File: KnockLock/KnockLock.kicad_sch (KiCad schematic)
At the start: 42 parts, among them IC1 ESP32-C3-WROOM-02-N4, IC2 LM2575-3.3WT, IC3 MC74HC74ADTR2G, J1 2477, J2 UJ20-C-H-G-TH-P16-TR, J3 TBP04R12-500-03BE, Q1 IRLML6402TRPBF, Q2 BC547B, Q3 BC547B, U1 ADXL345BCCZ-RL7

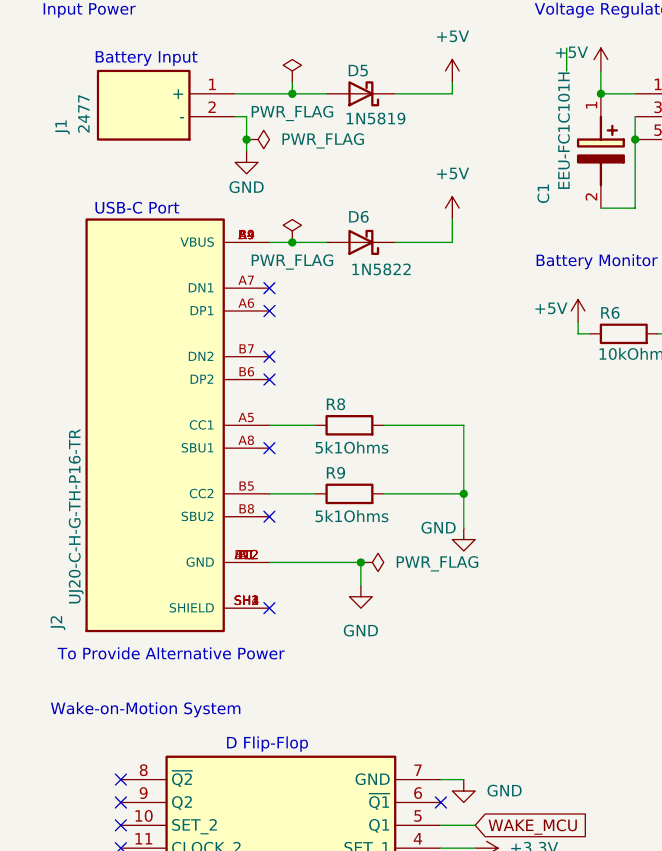
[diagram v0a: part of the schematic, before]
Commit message: Shifting to USB port, so added port and UART, but UART not connected
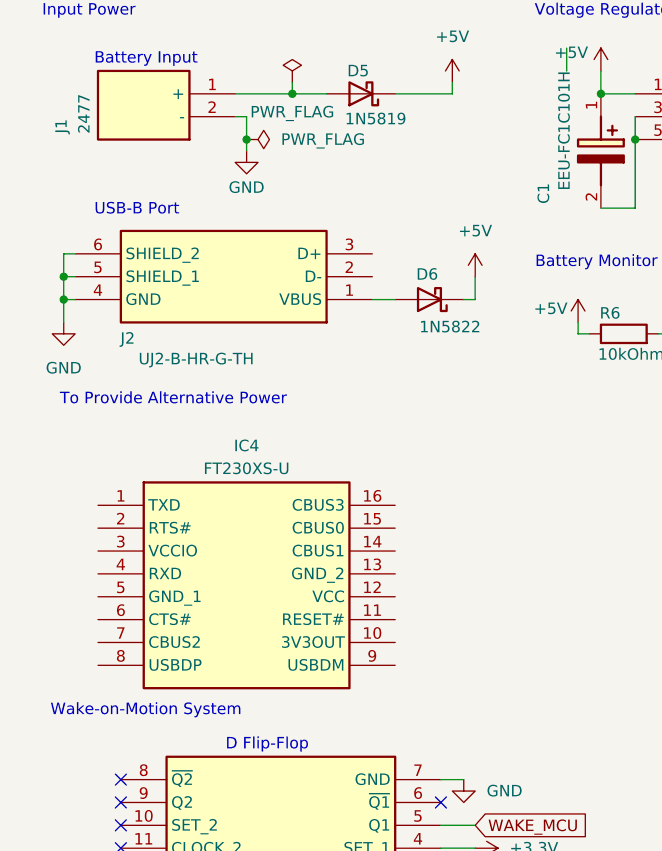
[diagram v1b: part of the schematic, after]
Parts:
- removed J2: UJ20-C-H-G-TH-P16-TR, UJ20-C-H-G-TH-P16-TR:SAMESKY_UJ20-C-H-G-TH-P16-TR, symbol UJ20-C-H-G-TH-P16-TR:UJ20-C-H-G-TH-P16-TR
- removed R8, R9: 5k1Ohms, symbol Device:R
- added IC4: FT230XS-U, SOP64P599X175-16N, symbol SamacSys_Parts:FT230XS-U
- added J2: UJ2-B-HR-G-TH, UJ2BHRGTH, symbol SamacSys_Parts:UJ2-B-HR-G-TH
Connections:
- net GND: now also J2.4 (GND), J2.5 (SHIELD_1), J2.6 (SHIELD_2)
- net at D6.2 (A): now also J2.1 (VBUS)
- no-connect marks 30 -> 23
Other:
- note added: "USB-B Port"
- note removed: "USB-C Port"
- moved on the sheet: D6

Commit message: Started Programming Interface
- we need to be careful with the IO pin logic so we can use basic buttons to enter programming mode or if we should try to use transistors (maybe also use the other side of the D flip flop)
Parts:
- added J4: UART, Connector_PinHeader_2.54mm:PinHeader_1x02_P2.54mm_Vertical, symbol Connector_Generic:Conn_01x02
- added SW1, SW2: SW_Push, symbol Switch:SW_Push
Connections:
- net FRESET: now also IC1.15 (IO3); no longer IC1.8 (IO9)
- net GND: now also SW1.1, SW2.1
- net RX: now reaches IC1.11 (RXD)
- net RX: now also J4.1 (Pin_1)
- net TX: now reaches IC1.12 (TXD)
- net TX: now also J4.2 (Pin_2)
- net MOSFET: no longer names the net of IC1.7 (IO8)
- net WAKE_MCU renamed MRESET
- net MRESET: now also SW1.2
- new net BOOT: IC1.8 (IO9), SW2.2
- no-connect marks 23 -> 21
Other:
- note added: "NPN Not Gate for Flip Flop Reset"
- note added: "Programming Interface"
- note added: "Turns off MCU"
- moved on the sheet: IC1, R1, R2

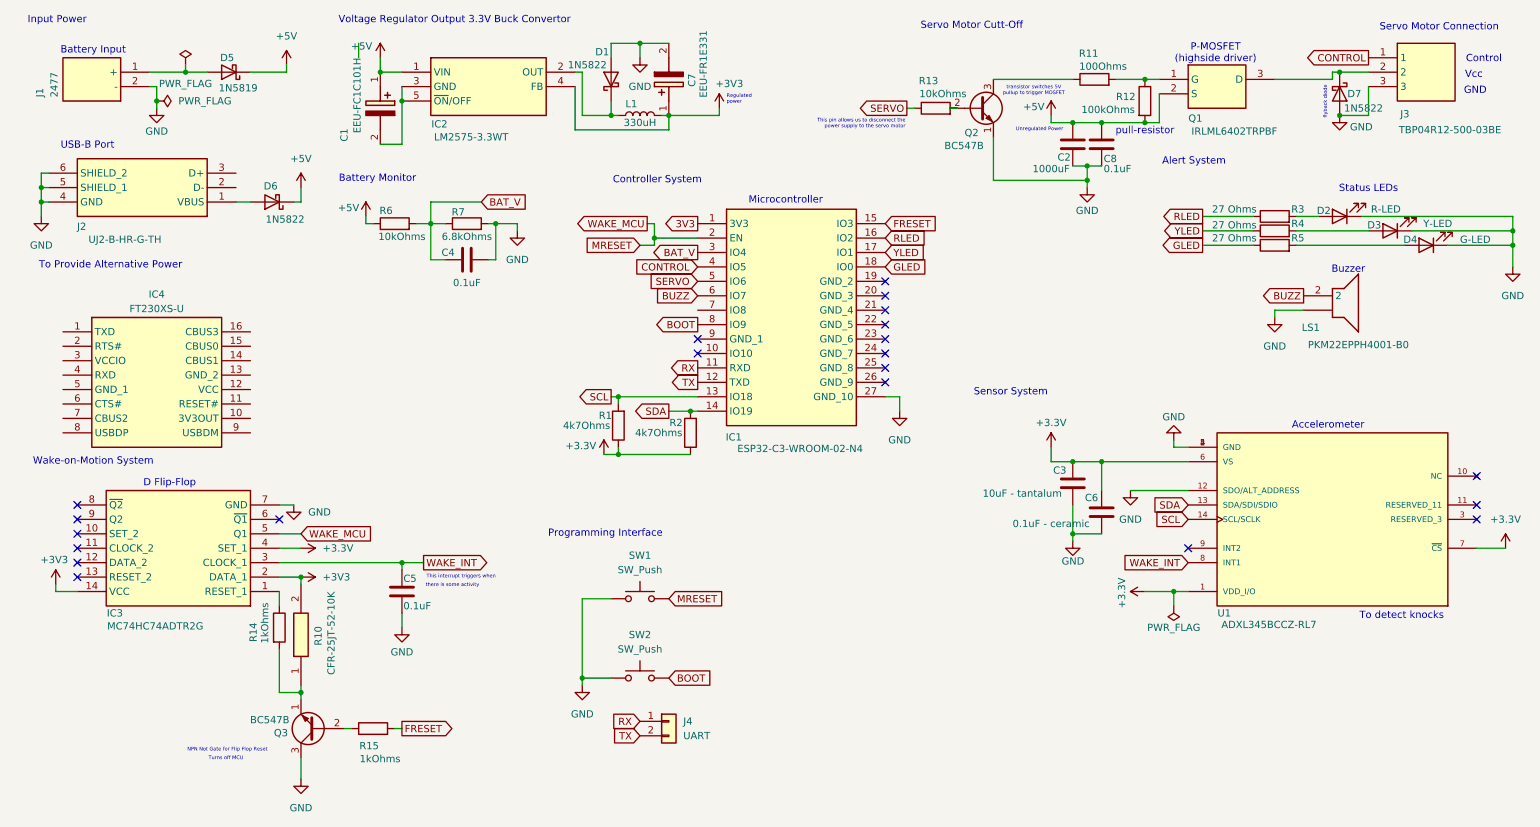
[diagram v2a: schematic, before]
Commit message: Reorganized, fixed pwr flags
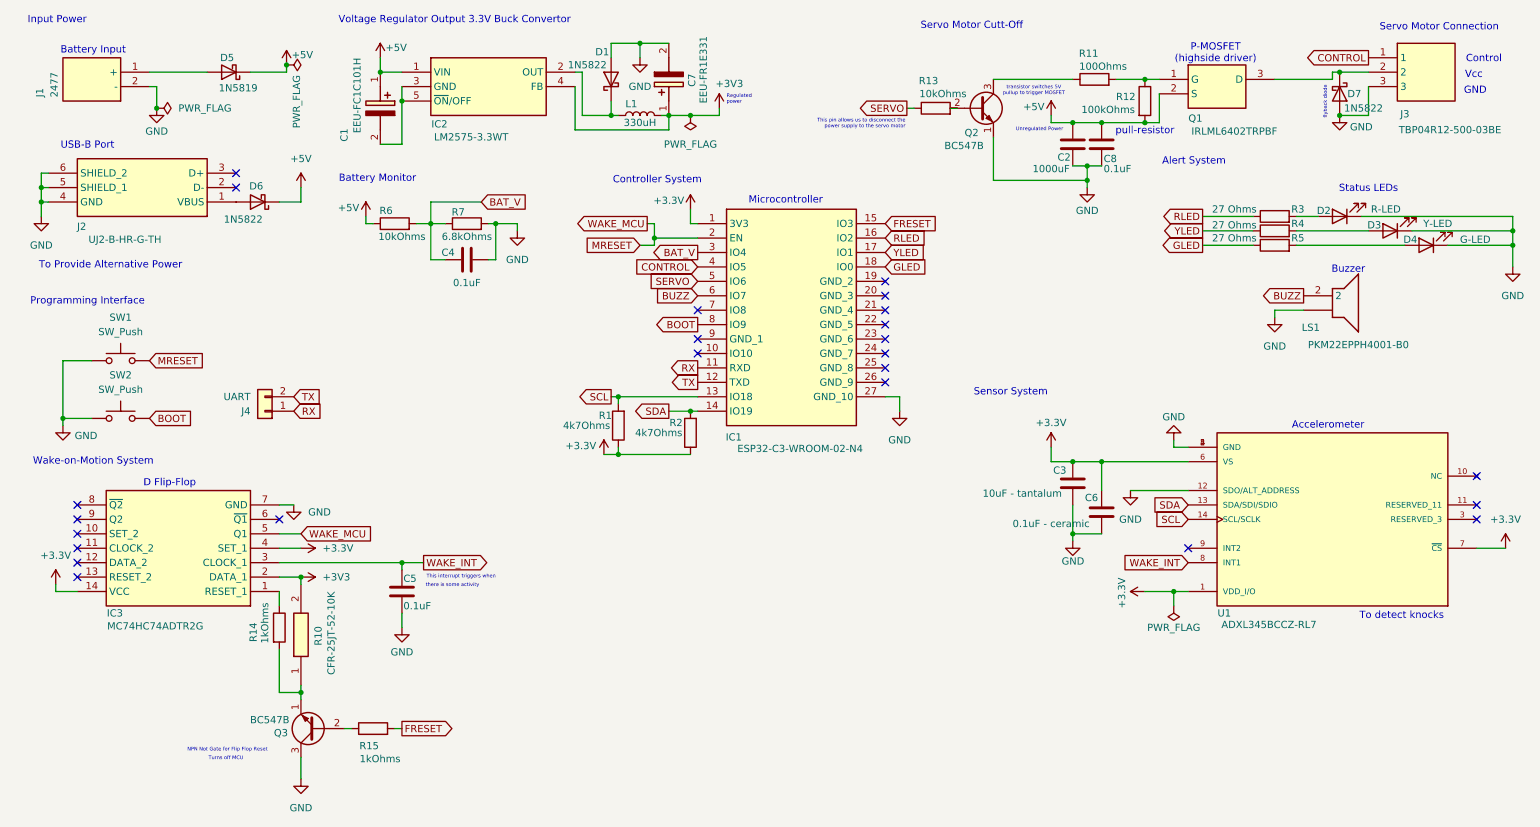
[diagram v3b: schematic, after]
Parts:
- removed IC4: FT230XS-U, SOP64P599X175-16N, symbol SamacSys_Parts:FT230XS-U
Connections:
- net 3V3 is gone; now on net +3.3V: IC1.1 (3V3)
- net +3.3V: now also IC3.14 (VCC)
- net +3V3: no longer IC3.14 (VCC)
- no-connect marks 21 -> 24
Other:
- moved on the sheet: D6, J4, SW1, SW2
